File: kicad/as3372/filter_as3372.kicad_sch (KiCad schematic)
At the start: 69 parts, among them Q1 MMBT3904, Q2 MMBT3904, Q3 MMBT3904, U11 DG442xY, U18 NE5532, U19 L79L05_TO92, U5 TL072, U8 AS3372

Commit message: getting close
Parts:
- R24: value 20k -> 24k; LCSC Part C4184 -> C23352
- R64: value 47k -> 24k; LCSC Part C25819 -> C23352
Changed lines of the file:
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@@
       (effects (font (size 1.27 1.27)) (justify right))
     )
-    (property "Value" "47k" (id 1) (at 221.488 96.9522 0)
+    (property "Value" "24k" (id 1) (at 221.488 96.9522 0)
       (effects (font (size 1.27 1.27)) (justify right))
     )
@@
       (effects (font (size 1.27 1.27)) hide)
     )
-    (property "LCSC Part" "C25819" (id 4) (at 219.71 95.25 0)
+    (property "LCSC Part" "C23352" (id 4) (at 219.71 95.25 0)
       (effects (font (size 1.27 1.27)) hide)
     )
@@
     (in_bom yes) (on_board yes)
     (property "Reference" "R24" (id 0) (at 80.01 129.54 90))
-    (property "Value" "20k" (id 1) (at 80.01 132.08 90))
+    (property "Value" "24k" (id 1) (at 80.01 132.08 90))
     (property "Footprint" "Resistor_SMD:R_0603_1608Metric" (id 2) (at 80.01 132.842 90)
       (effects (font (size 1.27 1.27)) hide)
@@
       (effects (font (size 1.27 1.27)) hide)
     )
-    (property "LCSC Part" "C4184" (id 4) (at 80.01 134.62 0)
-      (effects (font (size 1.27 1.27)) hide)
-    )
+    (property "LCSC Part" "C23352" (id 4) (at 80.01 134.62 0)
+      (effects (font (size 1.27 1.27)) hide)
+    )

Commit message: z3372 v0.2 release to manufacturing
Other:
- note added: "Resonance modulation: invert with gain of 1.0 Idea being that if one modulates filter cutoff _and_ resonance, you want res high while cutoff is low and vice versa."
- note removed: "Resonance modulation: invert with gain of 1.0 Idea being that if one modulates filter cutoff and resonance, you want res high while cutoff is low and vice versa."
- note removed: "Spares"
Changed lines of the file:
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@@
   (title_block
     (title "Z3372 Signal Processing")
-    (rev "0.1")
+    (rev "0.2")
     (company "Zoxnoxious Engineering")
   )
@@
     (stroke (width 0) (type default) (color 0 0 0 0))
   )
-  (polyline (pts (xy 384.175 182.245) (xy 414.655 182.245))
-    (stroke (width 0) (type default) (color 0 0 0 0))
-  )
   (wire (pts (xy 214.63 220.98) (xy 214.63 223.52))
     (stroke (width 0) (type default) (color 0 0 0 0))
@@
     (stroke (width 0) (type default) (color 0 0 0 0))
   )
-  (polyline (pts (xy 384.175 182.245) (xy 384.175 230.505))
-    (stroke (width 0) (type default) (color 0 0 0 0))
-  )
   (wire (pts (xy 54.61 226.06) (xy 58.42 226.06))
     (stroke (width 0) (type default) (color 0 0 0 0))
@@
     (stroke (width 0) (type default) (color 0 0 0 0))
   )
-  (polyline (pts (xy 414.655 182.245) (xy 414.655 230.505))
-    (stroke (width 0) (type default) (color 0 0 0 0))
-  )
   (wire (pts (xy 170.18 102.235) (xy 170.18 111.76))
     (stroke (width 0) (type default) (color 0 0 0 0))
@@
     (stroke (width 0) (type default) (color 0 0 0 0))
   )
-  (polyline (pts (xy 414.655 230.505) (xy 384.175 230.505))
-    (stroke (width 0) (type default) (color 0 0 0 0))
-  )
   (wire (pts (xy 170.18 111.76) (xy 170.18 119.38))
     (stroke (width 0) (type default) (color 0 0 0 0))
   )
-  (text "Spares" (at 387.985 186.055 0)
-    (effects (font (size 1.27 1.27)) (justify left bottom))
-  )
-  (text "Resonance modulation:\ninvert with gain of 1.0\nIdea being that if one modulates filter cutoff and resonance,\nyou want res high while cutoff is low and vice versa."
+  (text "Resonance modulation:\ninvert with gain of 1.0\nIdea being that if one modulates filter cutoff _and_ resonance,\nyou want res high while cutoff is low and vice versa."
     (at 217.17 29.21 0)
     (effects (font (size 1.27 1.27)) (justify left bottom))

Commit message: add part number for cap c18 c19
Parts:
- C18, C19: LCSC Part (none) -> C107115
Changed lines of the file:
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@@
       (effects (font (size 1.27 1.27)) hide)
     )
-    (property "LCSC Part" "" (id 4) (at 243.84 113.665 0)
+    (property "LCSC Part" "C107115" (id 4) (at 243.84 113.665 0)
       (effects (font (size 1.27 1.27)) hide)
     )
@@
       (effects (font (size 1.27 1.27)) hide)
     )
-    (property "LCSC Part" "" (id 4) (at 242.57 82.55 0)
-      (effects (font (size 1.27 1.27)) hide)
-    )
+    (property "LCSC Part" "C107115" (id 4) (at 242.57 82.55 0)
+      (effects (font (size 1.27 1.27)) hide)
+    )

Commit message: start making v0.3 changes
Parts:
- removed C14: 4.7u, Capacitor_THT:CP_Radial_D4.0mm_P1.50mm, symbol Device:C_Polarized
- removed C16: 2.2u, Capacitor_THT:CP_Radial_D4.0mm_P1.50mm, symbol Device:C_Polarized
- added C14, C16: 2.2u, Capacitor_THT:C_Rect_L7.2mm_W5.5mm_P5.00mm_FKS2_FKP2_MKS2_MKP2, symbol Device:C
- added C23: 2.2u, Capacitor_THT:CP_Radial_D4.0mm_P1.50mm, symbol Device:C_Polarized
- U19: footprint Package_TO_SOT_THT:TO-92_Inline -> Package_TO_SOT_THT:TO-92_Inline_Wide
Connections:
- net VCF_RAW: now also C16.2
- net VCF_SIG1: now also C23.1; no longer R22.2
- net at R32.1: now also C14.2
- net at U8.23 (VCF_Out): now also C14.1, C16.1
- new net: C23.2, R22.2
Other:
- note added: "C14, C16: Film cap or similar"
- note removed: "CONSIDER SCI P600 TRIMMER"
- moved on the sheet: R22
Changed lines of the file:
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@@
+    (stroke (width 0) (type default) (color 0 0 0 0))
+  )
+  (wire (pts (xy 92.71 64.77) (xy 96.52 64.77))
     (stroke (width 0) (type default) (color 0 0 0 0))
   )
@@
     (stroke (width 0) (type default) (color 0 0 0 0))
   )
+  (wire (pts (xy 104.14 64.77) (xy 106.68 64.77))
+    (stroke (width 0) (type default) (color 0 0 0 0))
+  )
   (wire (pts (xy 235.585 226.06) (xy 235.585 227.965))
     (stroke (width 0) (type default) (color 0 0 0 0))
@@
   )
   (wire (pts (xy 121.92 121.92) (xy 121.92 125.73))
-    (stroke (width 0) (type default) (color 0 0 0 0))
-  )
-  (wire (pts (xy 92.71 64.77) (xy 106.68 64.77))
     (stroke (width 0) (type default) (color 0 0 0 0))
   )
@@
     (effects (font (size 1.27 1.27)) (justify left bottom))
   )
-  (text "CONSIDER SCI P600 TRIMMER" (at 59.055 111.76 0)
+  (text "C14, C16: Film cap or similar" (at 165.1 95.25 0)
     (effects (font (size 1.27 1.27)) (justify left bottom))
   )
@@
     (pin "2")
   )
+  (symbol (lib_id "Device:C") (at 161.29 97.79 90) (unit 1)
+    (in_bom yes) (on_board yes) (fields_autoplaced)
+    (property "Reference" "C16" (id 0) (at 161.29 91.9312 90))
+    (property "Value" "2.2u" (id 1) (at 161.29 94.4681 90))
+    (property "Footprint" "Capacitor_THT:C_Rect_L7.2mm_W5.5mm_P5.00mm_FKS2_FKP2_MKS2_MKP2" (id 2) (at 165.1 96.8248 0)
+      (effects (font (size 1.27 1.27)) hide)
+    )
+    (property "Datasheet" "~" (id 3) (at 161.29 97.79 0)
+      (effects (font (size 1.27 1.27)) hide)
+    )
+    (property "Digikey" "MKS2B042201F00KSSD" (id 4) (at 161.29 97.79 0)
+      (effects (font (size 1.27 1.27)) hide)
+    )
+    (pin "1")
+    (pin "2")
+  )
+  (symbol (lib_id "Device:C") (at 151.13 104.14 0) (unit 1)
+    (in_bom yes) (on_board yes) (fields_autoplaced)
+    (property "Reference" "C14" (id 0) (at 154.051 103.3053 0)
+      (effects (font (size 1.27 1.27)) (justify left))
+    )
+    (property "Value" "2.2u" (id 1) (at 154.051 105.8422 0)
+      (effects (font (size 1.27 1.27)) (justify left))
+    )
+    (property "Footprint" "Capacitor_THT:C_Rect_L7.2mm_W5.5mm_P5.00mm_FKS2_FKP2_MKS2_MKP2" (id 2) (at 152.0952 107.95 0)
+      (effects (font (size 1.27 1.27)) hide)
+    )
+    (property "Datasheet" "~" (id 3) (at 151.13 104.14 0)
+      (effects (font (size 1.27 1.27)) hide)
+    )
+    (property "Digikey" "MKS2B042201F00KSSD" (id 4) (at 151.13 104.14 0)
+      (effects (font (size 1.27 1.27)) hide)
+    )
+    (pin "1")
+    (pin "2")
+  )
   (symbol (lib_id "Transistor_BJT:MMBT3904") (at 49.53 226.06 180) (unit 1)
     (in_bom yes) (on_board yes)
@@
     (pin "1")
   )
-  (symbol (lib_id "Device:C_Polarized") (at 161.29 97.79 90) (unit 1)
-    (in_bom yes) (on_board yes) (fields_autoplaced)
-    (property "Reference" "C16" (id 0) (at 160.401 91.9312 90))
-    (property "Value" "2.2u" (id 1) (at 160.401 94.4681 90))
-    (property "Footprint" "Capacitor_THT:CP_Radial_D4.0mm_P1.50mm" (id 2) (at 165.1 96.8248 0)
-      (effects (font (size 1.27 1.27)) hide)
-    )
-    (property "Datasheet" "~" (id 3) (at 161.29 97.79 0)
-      (effects (font (size 1.27 1.27)) hide)
-    )
-    (property "Digikey" "1189-4114-ND" (id 4) (at 161.29 97.79 0)
-      (effects (font (size 1.27 1.27)) hide)
-    )
-    (pin "1")
-    (pin "2")
-  )
   (symbol (lib_id "power:GND") (at 235.585 227.965 0) (unit 1)
     (in_bom yes) (on_board yes) (fields_autoplaced)
@@
     (pin "2")
   )
-  (symbol (lib_id "Device:R") (at 88.9 64.77 270) (unit 1)
-    (in_bom yes) (on_board yes) (fields_autoplaced)
-    (property "Reference" "R22" (id 0) (at 88.9 60.0542 90))
-    (property "Value" "22k" (id 1) (at 88.9 62.5911 90))
-    (property "Footprint" "Resistor_SMD:R_0603_1608Metric" (id 2) (at 88.9 62.992 90)
-      (effects (font (size 1.27 1.27)) hide)
-    )
-    (property "Datasheet" "~" (id 3) (at 88.9 64.77 0)
-      (effects (font (size 1.27 1.27)) hide)
-    )
-    (property "LCSC Part" "C31850" (id 4) (at 88.9 64.77 0)
+  (symbol (lib_id "Device:R") (at 100.33 64.77 270) (unit 1)
+    (in_bom yes) (on_board yes) (fields_autoplaced)
+    (property "Reference" "R22" (id 0) (at 100.33 60.0542 90))
+    (property "Value" "22k" (id 1) (at 100.33 62.5911 90))
+    (property "Footprint" "Resistor_SMD:R_0603_1608Metric" (id 2) (at 100.33 62.992 90)
+      (effects (font (size 1.27 1.27)) hide)
+    )
+    (property "Datasheet" "~" (id 3) (at 100.33 64.77 0)
+      (effects (font (size 1.27 1.27)) hide)
+    )
+    (property "LCSC Part" "C31850" (id 4) (at 100.33 64.77 0)
       (effects (font (size 1.27 1.27)) hide)
     )
@@
     (pin "8")
   )
-  (symbol (lib_id "Device:C_Polarized") (at 151.13 104.14 0) (unit 1)
-    (in_bom yes) (on_board yes) (fields_autoplaced)
-    (property "Reference" "C14" (id 0) (at 154.051 102.4163 0)
-      (effects (font (size 1.27 1.27)) (justify left))
-    )
-    (property "Value" "4.7u" (id 1) (at 154.051 104.9532 0)
-      (effects (font (size 1.27 1.27)) (justify left))
-    )
-    (property "Footprint" "Capacitor_THT:CP_Radial_D4.0mm_P1.50mm" (id 2) (at 152.0952 107.95 0)
-      (effects (font (size 1.27 1.27)) hide)
-    )
-    (property "Datasheet" "~" (id 3) (at 151.13 104.14 0)
-      (effects (font (size 1.27 1.27)) hide)
-    )
-    (property "Digikey" "1189-4113-ND" (id 4) (at 151.13 104.14 0)
-      (effects (font (size 1.27 1.27)) hide)
-    )
-    (pin "1")
-    (pin "2")
-  )
   (symbol (lib_id "Regulator_Linear:L79L05_TO92") (at 255.27 237.49 0) (unit 1)
     (in_bom yes) (on_board yes) (fields_autoplaced)
     (property "Reference" "U19" (id 0) (at 255.27 241.4254 0))
     (property "Value" "L79L05_TO92" (id 1) (at 255.27 243.9623 0))
-    (property "Footprint" "Package_TO_SOT_THT:TO-92_Inline" (id 2) (at 255.27 242.57 0)
+    (property "Footprint" "Package_TO_SOT_THT:TO-92_Inline_Wide" (id 2) (at 255.27 242.57 0)
       (effects (font (size 1.27 1.27) italic) hide)
     )
@@
       (effects (font (size 1.27 1.27)) hide)
     )
+    (pin "1")
+    (pin "2")
+  )
+  (symbol (lib_id "Device:C_Polarized") (at 88.9 64.77 90) (unit 1)
+    (in_bom yes) (on_board yes) (fields_autoplaced)
+    (property "Reference" "C23" (id 0) (at 88.011 58.9112 90))
+    (property "Value" "2.2u" (id 1) (at 88.011 61.4481 90))
+    (property "Footprint" "Capacitor_THT:CP_Radial_D4.0mm_P1.50mm" (id 2) (at 92.71 63.8048 0)
+      (effects (font (size 1.27 1.27)) hide)
+    )
+    (property "Datasheet" "~" (id 3) (at 88.9 64.77 0)
+      (effects (font (size 1.27 1.27)) hide)
+    )
+    (property "Digikey" "1189-4114-ND" (id 4) (at 88.9 64.77 0)
+      (effects (font (size 1.27 1.27)) hide)
+    )

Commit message: mods for v0.3
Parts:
- removed R16: 1k, Resistor_SMD:R_0603_1608Metric, symbol Device:R
- C18, C19: footprint Capacitor_SMD:C_0805_2012Metric -> Capacitor_SMD:C_0603_1608Metric; LCSC Part C107115 -> C1663
- C38: value 4.7u -> 22u; footprint Capacitor_SMD:C_0805_2012Metric -> Capacitor_SMD:C_1206_3216Metric; LCSC Part C1779 -> C12891
- R13: value 47k -> 82k; LCSC Part C25819 -> C23254
- R32: value 24k -> 27k; LCSC Part C23352 -> C22967
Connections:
- net GND: now also R71.2
- net NOISE_CV: now also Q3.1 (B)
- net at C38.2, Q3.3 (C): no longer R71.2
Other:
- note added: "C11, C12, C15, C17: NP0 or better"
- note removed: "Diode is to protect input from sources less than -5 Volts. Not done on other pins since thye're divided down to within range."
- moved on the sheet: C38, Q3, R13, R14, R15, R21, R71, TP1, TP13, TP2

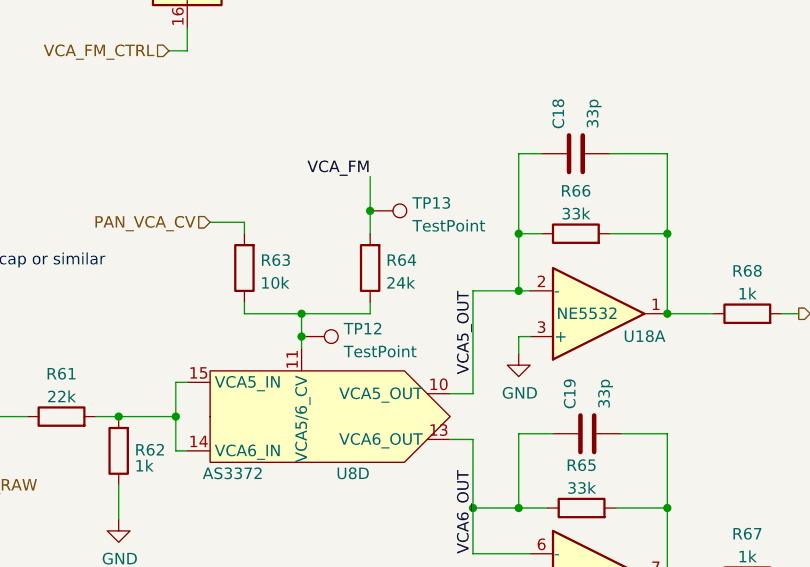
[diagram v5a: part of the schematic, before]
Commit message: add proper component part numbers
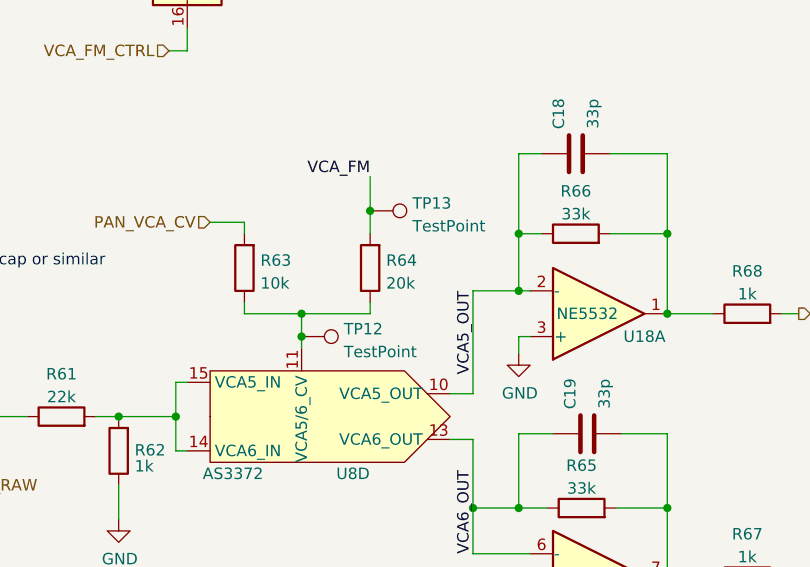
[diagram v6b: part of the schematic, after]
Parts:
- R64: value 24k -> 20k; LCSC Part C23352 -> C4184
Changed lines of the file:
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@@
       (effects (font (size 1.27 1.27)) (justify right))
     )
-    (property "Value" "24k" (id 1) (at 221.488 96.9522 0)
+    (property "Value" "20k" (id 1) (at 221.488 96.9522 0)
       (effects (font (size 1.27 1.27)) (justify right))
     )
@@
       (effects (font (size 1.27 1.27)) hide)
     )
-    (property "LCSC Part" "C23352" (id 4) (at 219.71 95.25 0)
+    (property "LCSC Part" "C4184" (id 4) (at 219.71 95.25 0)
       (effects (font (size 1.27 1.27)) hide)
     )

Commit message: update caps based on production
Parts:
- C11, C12, C17: LCSC Part C342800 -> C76628
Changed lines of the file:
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@@
       (effects (font (size 1.27 1.27)) hide)
     )
-    (property "LCSC Part" "C342800" (id 4) (at 107.95 118.11 0)
+    (property "LCSC Part" "C76628" (id 4) (at 107.95 118.11 0)
       (effects (font (size 1.27 1.27)) hide)
     )
@@
       (effects (font (size 1.27 1.27)) hide)
     )
-    (property "LCSC Part" "C342800" (id 4) (at 114.3 118.11 0)
+    (property "LCSC Part" "C76628" (id 4) (at 114.3 118.11 0)
       (effects (font (size 1.27 1.27)) hide)
     )
@@
       (effects (font (size 1.27 1.27)) hide)
     )
-    (property "LCSC Part" "C342800" (id 4) (at 121.92 118.11 0)
-      (effects (font (size 1.27 1.27)) hide)
-    )
+    (property "LCSC Part" "C76628" (id 4) (at 121.92 118.11 0)
+      (effects (font (size 1.27 1.27)) hide)
+    )
